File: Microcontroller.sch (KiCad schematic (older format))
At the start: 1 part

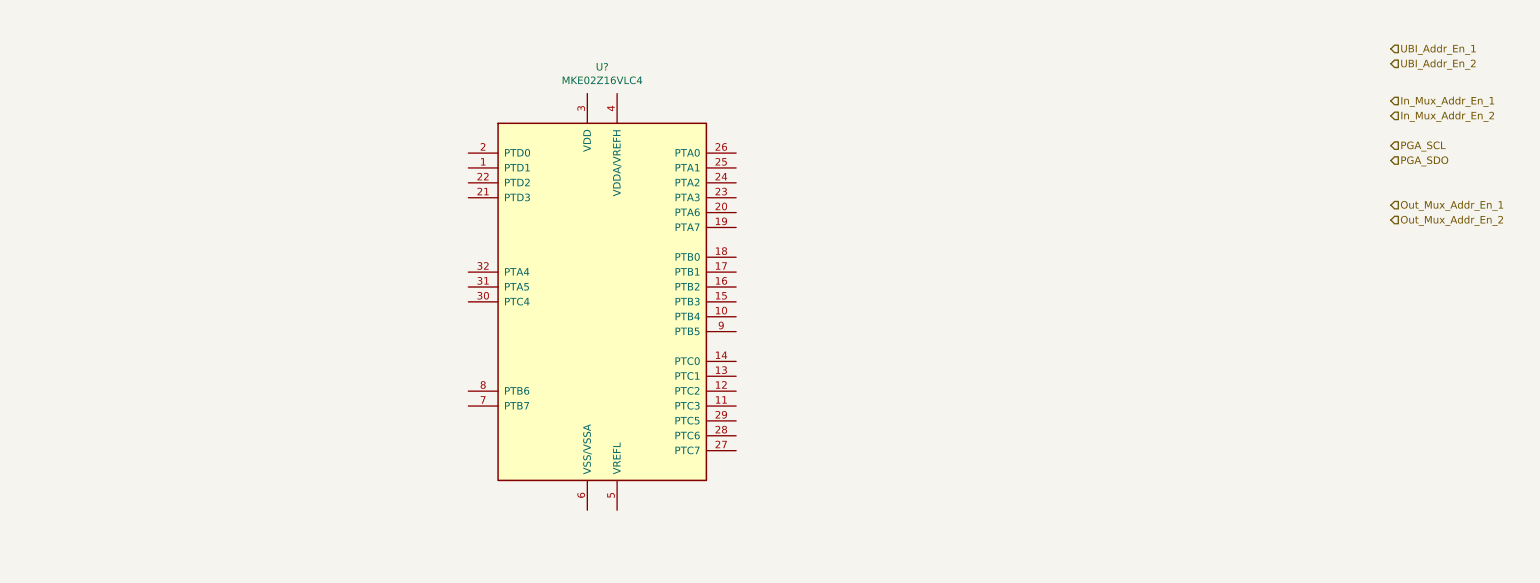
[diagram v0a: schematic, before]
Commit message: Add crystal and debug connector to MCU
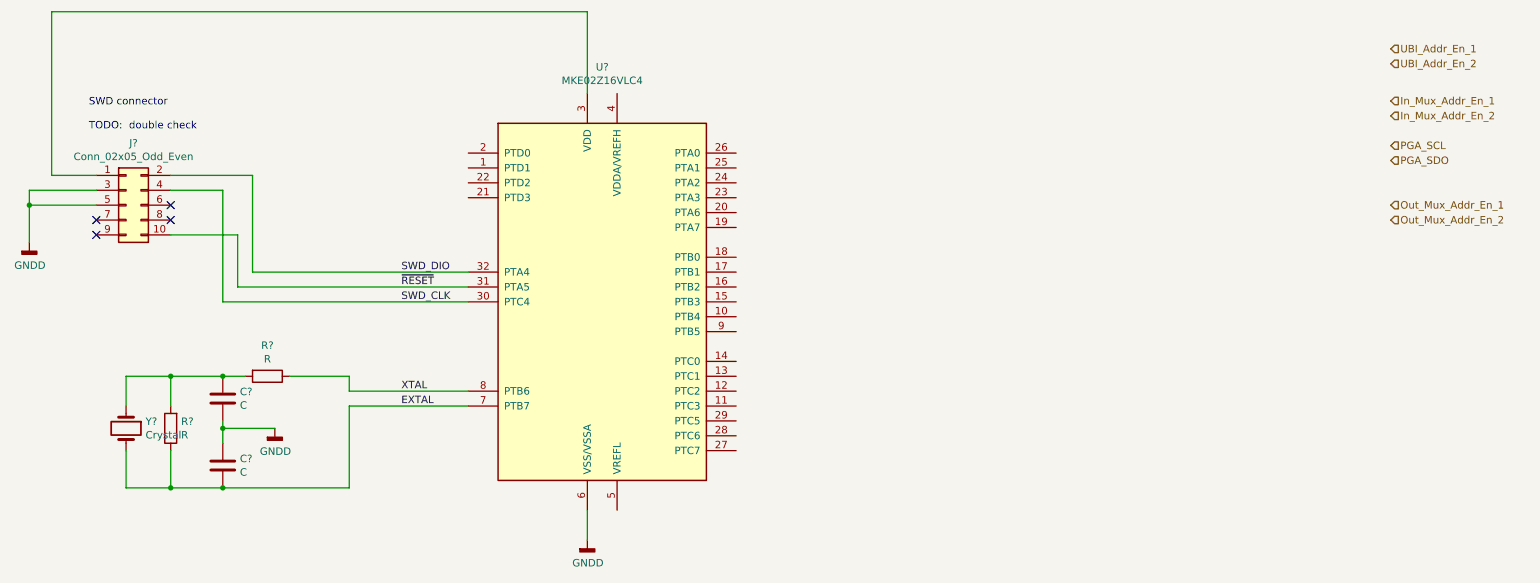
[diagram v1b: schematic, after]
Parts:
- added C? (x2): C, symbol Device:C
- added J?: Conn_02x05_Odd_Even, symbol Connector_Generic:Conn_02x05_Odd_Even
- added R? (x2): R, symbol Device:R
- added Y?: Crystal, symbol Device:Crystal
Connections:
- net at U?.3 (VDD): now also J?.1 (Pin_1)
- net SWD_CLK: now reaches U?.30 (PTC4)
- net SWD_CLK: now also J?.4 (Pin_4)
- net ~RESET: now reaches U?.31 (PTA5)
- net ~RESET: now also J?.10 (Pin_10)
- net SWD_DIO: now reaches U?.32 (PTA4)
- net SWD_DIO: now also J?.2 (Pin_2)
- net GNDD: now reaches U?.6 (VSS/VSSA)
- net GNDD: now also C?.1, C?.2, J?.3 (Pin_3), J?.5 (Pin_5)
- net EXTAL: now reaches U?.7 (PTB7)
- net EXTAL: now also C?.2, R?.1, Y?.2
- net XTAL: now reaches U?.8 (PTB6)
- net XTAL: now also R?.1
- new net: C?.1, R?.2, R?.2, Y?.1
- no-connect marks 0 -> 4
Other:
- note added: "SWD connector\n\nTODO: double check"
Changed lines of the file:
@@
 	1    0    0    -1
 $EndComp
+Text Label 3350 2950 0    50   ~ 0
+SWD_DIO
+Text Label 3350 3050 0    50   ~ 0
+~RESET
+Text Label 3350 3150 0    50   ~ 0
+SWD_CLK
+Wire Wire Line
+	3800 3750 3000 3750
+Wire Wire Line
+	3800 3850 3000 3850
+Text Label 3350 3750 0    50   ~ 0
+XTAL
+Text Label 3350 3850 0    50   ~ 0
+EXTAL
+$Comp
+L Device:R R?
+U 1 1 5E5F9376
+P 2450 3650
+F 0 "R?" V 2243 3650 50  0000 C CNN
+F 1 "R" V 2334 3650 50  0000 C CNN
+F 2 "" V 2380 3650 50  0001 C CNN
+F 3 "~" H 2450 3650 50  0001 C CNN
+	1    2450 3650
+	0    1    1    0
+$EndComp
+$Comp
+L Device:C C?
+U 1 1 5E5FA01D
+P 2150 3800
+F 0 "C?" H 2265 3846 50  0000 L CNN
+F 1 "C" H 2265 3755 50  0000 L CNN
+F 2 "" H 2188 3650 50  0001 C CNN
+F 3 "~" H 2150 3800 50  0001 C CNN
+	1    2150 3800
+	1    0    0    -1
+$EndComp
+$Comp
+L Device:C C?
+U 1 1 5E5FA5AF
+P 2150 4250
+F 0 "C?" H 2265 4296 50  0000 L CNN
+F 1 "C" H 2265 4205 50  0000 L CNN
+F 2 "" H 2188 4100 50  0001 C CNN
+F 3 "~" H 2150 4250 50  0001 C CNN
+	1    2150 4250
+	1    0    0    -1
+$EndComp
+$Comp
+L Device:R R?
+U 1 1 5E5FA7F8
+P 1800 4000
+F 0 "R?" H 1730 3954 50  0000 R CNN
+F 1 "R" H 1730 4045 50  0000 R CNN
+F 2 "" V 1730 4000 50  0001 C CNN
+F 3 "~" H 1800 4000 50  0001 C CNN
+	1    1800 4000
+	-1   0    0    1
+$EndComp
+$Comp
+L Device:Crystal Y?
+U 1 1 5E5FB285
+P 1500 4000
+F 0 "Y?" V 1454 4131 50  0000 L CNN
+F 1 "Crystal" V 1545 4131 50  0000 L CNN
+F 2 "" H 1500 4000 50  0001 C CNN
+F 3 "~" H 1500 4000 50  0001 C CNN
+	1    1500 4000
+	0    1    1    0
+$EndComp
+Wire Wire Line
+	3000 3750 3000 3650
+Wire Wire Line
+	3000 3650 2600 3650
+Wire Wire Line
+	2300 3650 2150 3650
+Wire Wire Line
+	2150 3950 2150 4000
+$Comp
+L power:GNDD #PWR?
+U 1 1 5E5FBF26
+P 2500 4000
+F 0 "#PWR?" H 2500 3750 50  0001 C CNN
+F 1 "GNDD" H 2504 3845 50  0000 C CNN
+F 2 "" H 2500 4000 50  0001 C CNN
+F 3 "" H 2500 4000 50  0001 C CNN
+	1    2500 4000
+	1    0    0    -1
+$EndComp
+$Comp
+L power:GNDD #PWR?
+U 1 1 5E5FC6D7
+P 4600 4750
+F 0 "#PWR?" H 4600 4500 50  0001 C CNN
+F 1 "GNDD" H 4604 4595 50  0000 C CNN
+F 2 "" H 4600 4750 50  0001 C CNN
+F 3 "" H 4600 4750 50  0001 C CNN
+	1    4600 4750
+	1    0    0    -1
+$EndComp
+Wire Wire Line
+	4600 4750 4600 4550
+Wire Wire Line
+	2500 4000 2150 4000
+Connection ~ 2150 4000
+Wire Wire Line
+	2150 4000 2150 4100
+Wire Wire Line
+	2150 4400 3000 4400
+Wire Wire Line
+	3000 4400 3000 3850
+Wire Wire Line
+	2150 3650 1800 3650
+Wire Wire Line
+	1500 3650 1500 3850
+Connection ~ 2150 3650
+Wire Wire Line
+	1500 4150 1500 4400
+Wire Wire Line
+	1500 4400 1800 4400
+Connection ~ 2150 4400
+Wire Wire Line
+	1800 4150 1800 4400
+Connection ~ 1800 4400
+Wire Wire Line
+	1800 4400 2150 4400
+Wire Wire Line
+	1800 3850 1800 3650
+Connection ~ 1800 3650
+Wire Wire Line
+	1800 3650 1500 3650
+$Comp
+L Connector_Generic:Conn_02x05_Odd_Even J?
+U 1 1 5E601875
+P 1500 2500
+F 0 "J?" H 1550 2917 50  0000 C CNN
+F 1 "Conn_02x05_Odd_Even" H 1550 2826 50  0000 C CNN
+F 2 "" H 1500 2500 50  0001 C CNN
+F 3 "~" H 1500 2500 50  0001 C CNN
+	1    1500 2500
+	1    0    0    -1
+$EndComp
+Wire Wire Line
+	4600 1750 4600 1200
+Wire Wire Line
+	4600 1200 1000 1200
+Wire Wire Line
+	1000 1200 1000 2300
+Wire Wire Line
+	1000 2300 1300 2300
+Wire Wire Line
+	1300 2400 850  2400
+Wire Wire Line
+	850  2400 850  2500
+Wire Wire Line
+	1300 2500 850  2500
+Connection ~ 850  2500
+Wire Wire Line
+	850  2500 850  2750
+$Comp
+L power:GNDD #PWR?
+U 1 1 5E605299
+P 850 2750
+F 0 "#PWR?" H 850 2500 50  0001 C CNN
+F 1 "GNDD" H 854 2595 50  0000 C CNN
+F 2 "" H 850 2750 50  0001 C CNN
+F 3 "" H 850 2750 50  0001 C CNN
+	1    850  2750
+	1    0    0    -1
+$EndComp
+NoConn ~ 1300 2600
+NoConn ~ 1300 2700
+NoConn ~ 1800 2500
+NoConn ~ 1800 2600
+Wire Wire Line
+	1800 2700 2250 2700
+Wire Wire Line
+	2250 2700 2250 3050
+Wire Wire Line
+	2250 3050 3800 3050
+Wire Wire Line
+	2350 2950 2350 2300
+Wire Wire Line
+	2350 2300 1800 2300
+Wire Wire Line
+	2350 2950 3800 2950
+Wire Wire Line
+	2150 3150 2150 2400
+Wire Wire Line
+	2150 2400 1800 2400
+Wire Wire Line
+	2150 3150 3800 3150
+Text Notes 1250 2000 0    50   ~ 0
+SWD connector\n\nTODO:  double check
 $EndSCHEMATC
